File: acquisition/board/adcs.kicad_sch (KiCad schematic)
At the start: 108 parts, among them U1 AD9251, U13 ICE40UP5K_QFN48, U2 XC7A50T-1FTG256C, U3 AD9251, U4 AD9251, U5 AD9251, U6 ICE40UP5K_QFN48

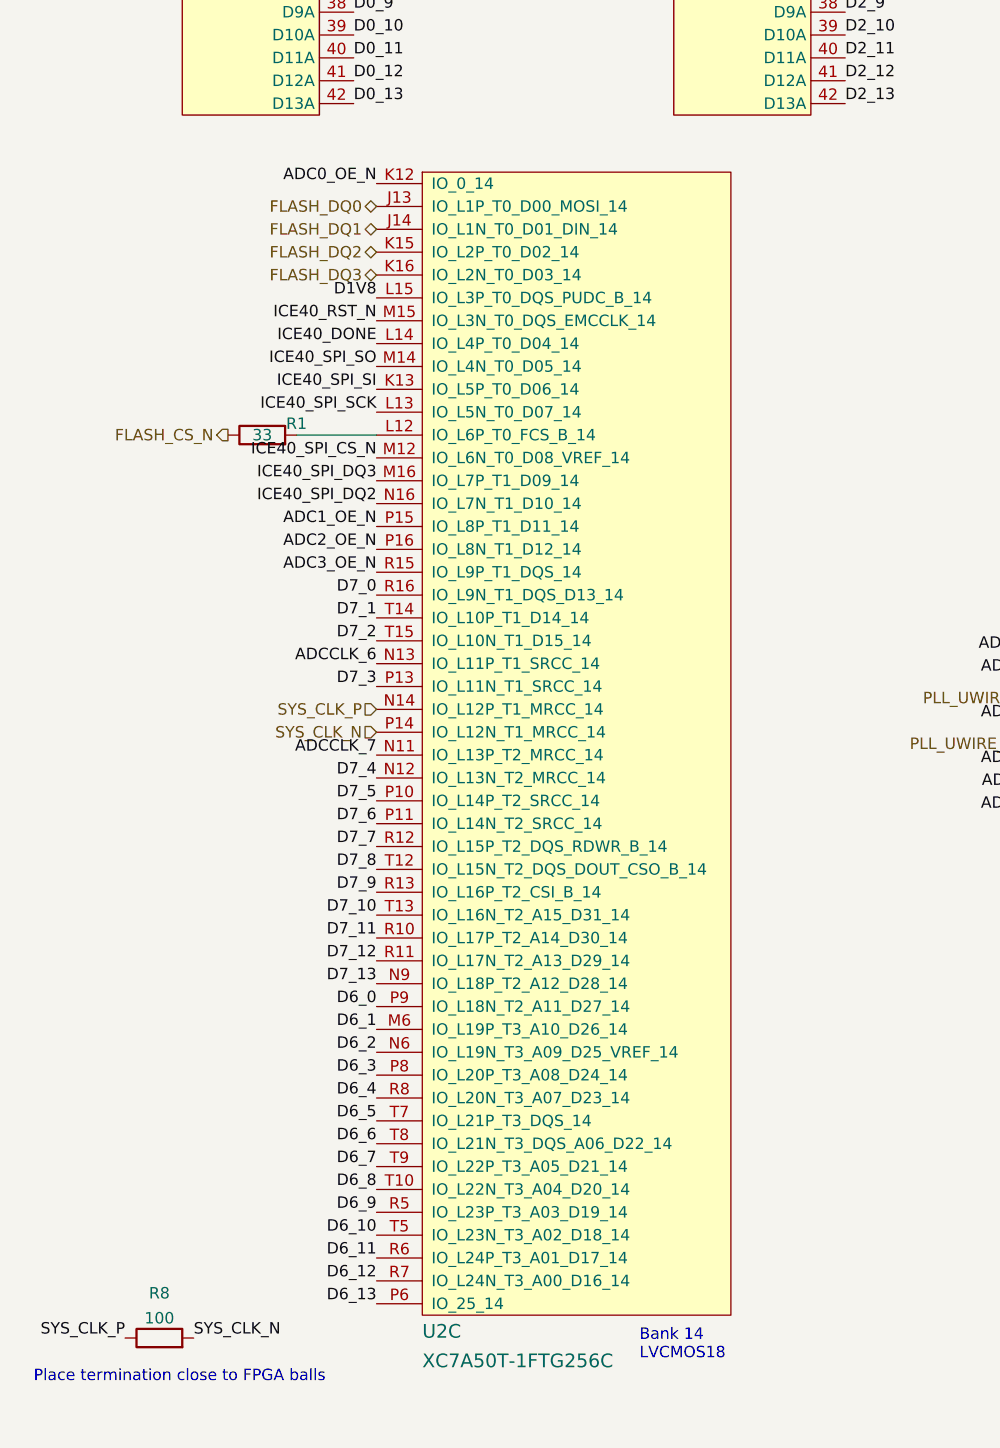
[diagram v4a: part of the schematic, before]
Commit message: Completed schematic after design review, ready for layout
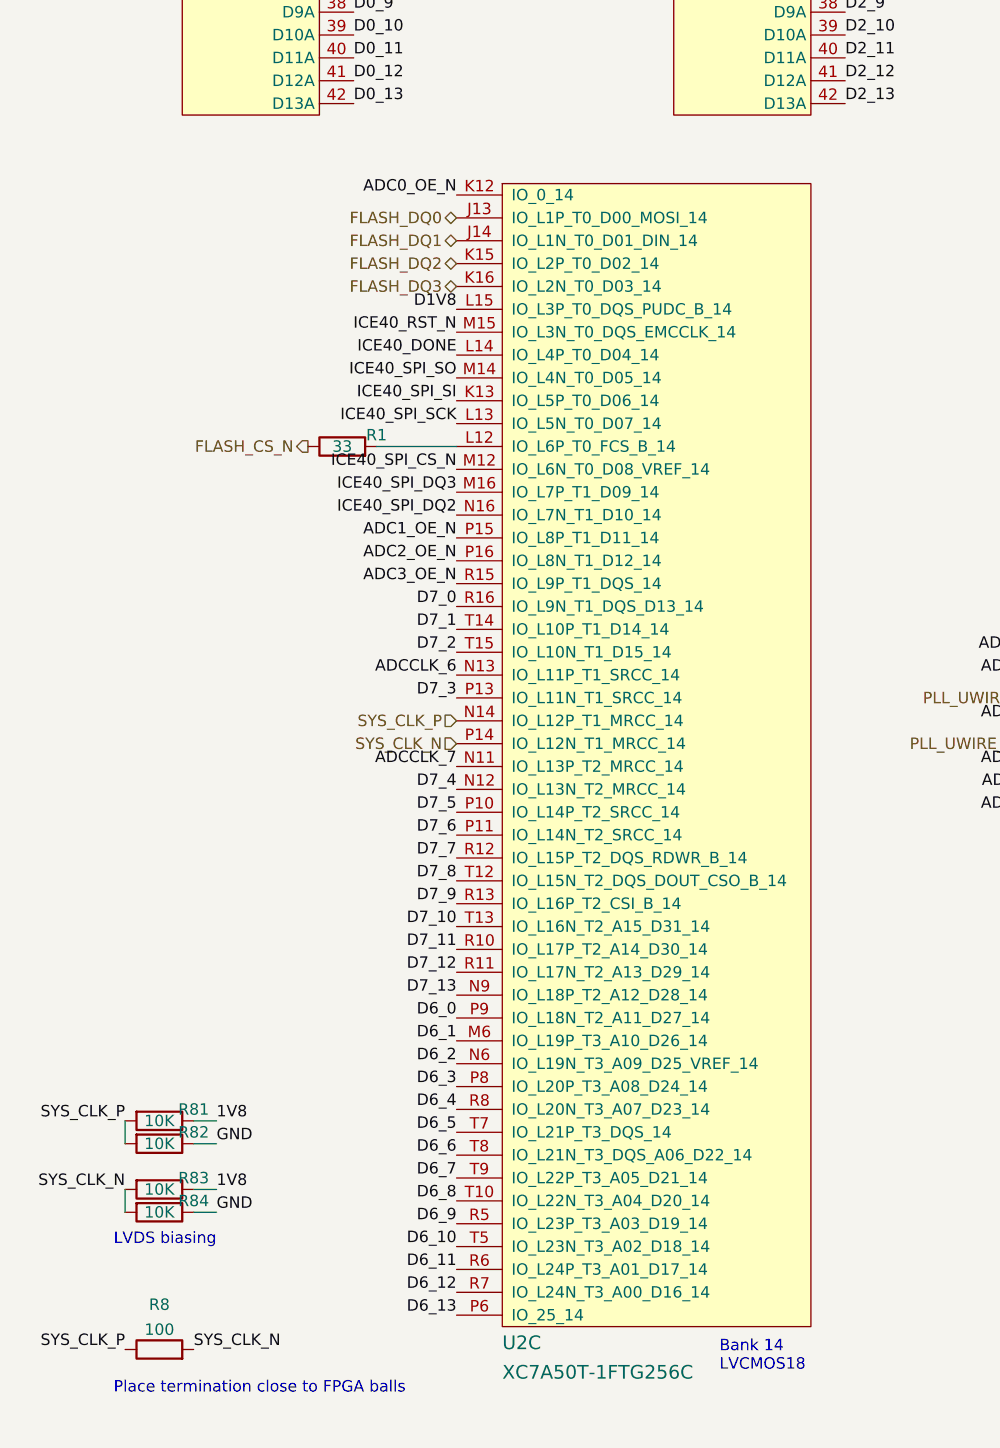
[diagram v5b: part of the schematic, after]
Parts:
- added R81, R82, R83, R84: 10K, azonenberg_pcb:EIA_0402_RES_NOSILK, symbol device:R
- C202, C203, C204, C205: footprint (none) -> azonenberg_pcb:EIA_0603_CAP_NOSILK
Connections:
- net 1V8: now also R81.1, R83.1
- net GND: now also R82.1, R84.1
- net SYS_CLK_N: now also R83.2, R84.2
- net SYS_CLK_P: now also R81.2, R82.2
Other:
- note added: "LVDS biasing"
- moved on the sheet: R1, R8, U2C

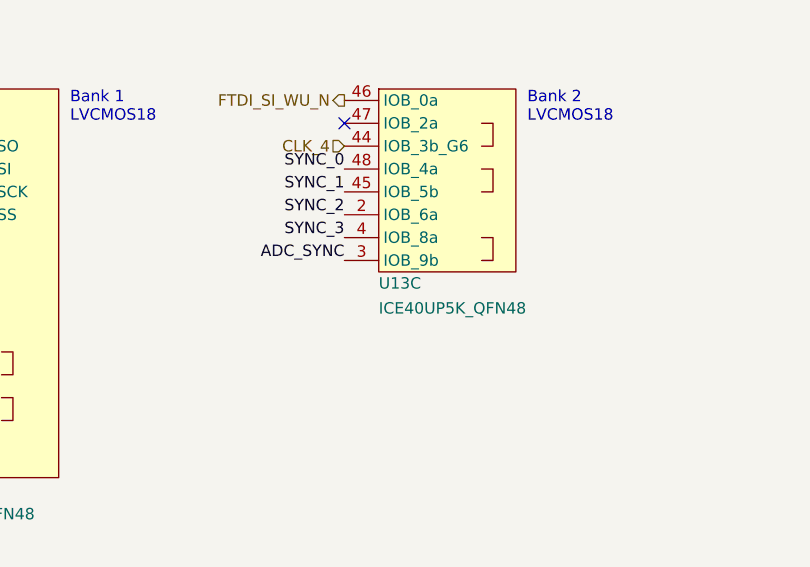
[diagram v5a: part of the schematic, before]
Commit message: Finished footprint assignment
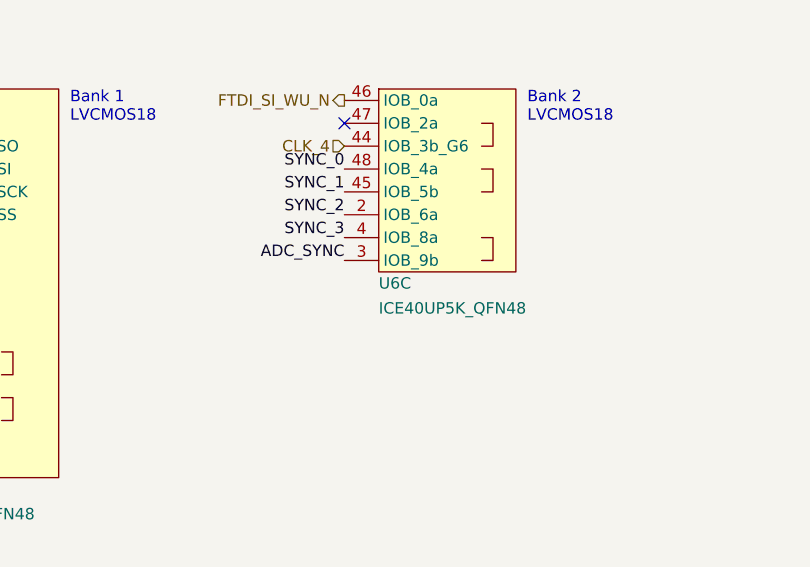
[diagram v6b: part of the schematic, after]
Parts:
- U1, U3, U4, U5: footprint (none) -> azonenberg_pcb:QFN_64_0.5MM_9x9MM
- U6: renamed from U13; footprint (none) -> azonenberg_pcb:QFN_48_0.5MM_7x7MM
- U6: footprint (none) -> azonenberg_pcb:QFN_48_0.5MM_7x7MM
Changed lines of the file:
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@@
   (title_block
     (title "Digitizer board")
-    (date "2022-07-17")
+    (date "2023-01-29")
     (rev "0.1")
     (company "A. Zonenberg")
@@
   (symbol (lib_id "lattice-azonenberg:ICE40UP5K_QFN48") (at 316.23 245.11 0) (unit 3)
     (in_bom yes) (on_board yes)
-    (property "Reference" "U13" (id 0) (at 316.23 246.38 0)
+    (property "Reference" "U6" (id 0) (at 316.23 246.38 0)
       (effects (font (size 1.27 1.27)) (justify left))
     )
@@
       (effects (font (size 1.27 1.27)) (justify left))
     )
-    (property "Footprint" "" (id 2) (at 316.23 245.11 0)
+    (property "Footprint" "azonenberg_pcb:QFN_48_0.5MM_7x7MM" (id 2) (at 316.23 245.11 0)
       (effects (font (size 1.27 1.27)) hide)
     )
@@
     (property "Reference" "U3" (id 0) (at 97.79 17.6743 0))
     (property "Value" "AD9251" (id 1) (at 97.79 20.4494 0))
-    (property "Footprint" "" (id 2) (at 87.63 86.36 0)
+    (property "Footprint" "azonenberg_pcb:QFN_64_0.5MM_9x9MM" (id 2) (at 87.63 86.36 0)
       (effects (font (size 1.27 1.27)) hide)
     )
@@
     (property "Reference" "U3" (id 0) (at 316.23 72.2843 0))
     (property "Value" "AD9251" (id 1) (at 316.23 75.0594 0))
-    (property "Footprint" "" (id 2) (at 308.61 121.92 0)
+    (property "Footprint" "azonenberg_pcb:QFN_64_0.5MM_9x9MM" (id 2) (at 308.61 121.92 0)
       (effects (font (size 1.27 1.27)) hide)
     )
@@
     (property "Reference" "U4" (id 0) (at 152.4 17.6743 0))
     (property "Value" "AD9251" (id 1) (at 152.4 20.4494 0))
-    (property "Footprint" "" (id 2) (at 142.24 86.36 0)
+    (property "Footprint" "azonenberg_pcb:QFN_64_0.5MM_9x9MM" (id 2) (at 142.24 86.36 0)
       (effects (font (size 1.27 1.27)) hide)
     )
@@
     (property "Reference" "U1" (id 0) (at 43.18 17.6743 0))
     (property "Value" "AD9251" (id 1) (at 43.18 20.4494 0))
-    (property "Footprint" "" (id 2) (at 33.02 86.36 0)
+    (property "Footprint" "azonenberg_pcb:QFN_64_0.5MM_9x9MM" (id 2) (at 33.02 86.36 0)
       (effects (font (size 1.27 1.27)) hide)
     )
@@
     (property "Reference" "U1" (id 0) (at 316.23 18.9443 0))
     (property "Value" "AD9251" (id 1) (at 316.23 21.7194 0))
-    (property "Footprint" "" (id 2) (at 308.61 68.58 0)
+    (property "Footprint" "azonenberg_pcb:QFN_64_0.5MM_9x9MM" (id 2) (at 308.61 68.58 0)
       (effects (font (size 1.27 1.27)) hide)
     )
@@
     (property "Reference" "U3" (id 0) (at 95.25 88.7943 0))
     (property "Value" "AD9251" (id 1) (at 95.25 91.5694 0))
-    (property "Footprint" "" (id 2) (at 87.63 138.43 0)
+    (property "Footprint" "azonenberg_pcb:QFN_64_0.5MM_9x9MM" (id 2) (at 87.63 138.43 0)
       (effects (font (size 1.27 1.27)) hide)
     )
@@
     (property "Reference" "U4" (id 0) (at 370.84 18.9443 0))
     (property "Value" "AD9251" (id 1) (at 370.84 21.7194 0))
-    (property "Footprint" "" (id 2) (at 363.22 68.58 0)
+    (property "Footprint" "azonenberg_pcb:QFN_64_0.5MM_9x9MM" (id 2) (at 363.22 68.58 0)
       (effects (font (size 1.27 1.27)) hide)
     )
@@
     (property "Reference" "U5" (id 0) (at 370.84 72.2843 0))
     (property "Value" "AD9251" (id 1) (at 370.84 75.0594 0))
-    (property "Footprint" "" (id 2) (at 363.22 121.92 0)
+    (property "Footprint" "azonenberg_pcb:QFN_64_0.5MM_9x9MM" (id 2) (at 363.22 121.92 0)
       (effects (font (size 1.27 1.27)) hide)
     )
@@
     (property "Reference" "U5" (id 0) (at 204.47 88.7943 0))
     (property "Value" "AD9251" (id 1) (at 204.47 91.5694 0))
-    (property "Footprint" "" (id 2) (at 196.85 138.43 0)
+    (property "Footprint" "azonenberg_pcb:QFN_64_0.5MM_9x9MM" (id 2) (at 196.85 138.43 0)
       (effects (font (size 1.27 1.27)) hide)
     )
@@
     (property "Reference" "U4" (id 0) (at 149.86 88.7943 0))
     (property "Value" "AD9251" (id 1) (at 149.86 91.5694 0))
-    (property "Footprint" "" (id 2) (at 142.24 138.43 0)
+    (property "Footprint" "azonenberg_pcb:QFN_64_0.5MM_9x9MM" (id 2) (at 142.24 138.43 0)
       (effects (font (size 1.27 1.27)) hide)
     )
@@
     (property "Reference" "U1" (id 0) (at 40.64 88.7943 0))
     (property "Value" "AD9251" (id 1) (at 40.64 91.5694 0))
-    (property "Footprint" "" (id 2) (at 33.02 138.43 0)
+    (property "Footprint" "azonenberg_pcb:QFN_64_0.5MM_9x9MM" (id 2) (at 33.02 138.43 0)
       (effects (font (size 1.27 1.27)) hide)
     )
@@
       (effects (font (size 1.27 1.27)) (justify left))
     )
-    (property "Footprint" "" (id 2) (at 261.62 267.97 0)
+    (property "Footprint" "azonenberg_pcb:QFN_48_0.5MM_7x7MM" (id 2) (at 261.62 267.97 0)
       (effects (font (size 1.27 1.27)) hide)
     )
@@
     (property "Reference" "U5" (id 0) (at 207.01 17.6743 0))
     (property "Value" "AD9251" (id 1) (at 207.01 20.4494 0))
-    (property "Footprint" "" (id 2) (at 196.85 86.36 0)
+    (property "Footprint" "azonenberg_pcb:QFN_64_0.5MM_9x9MM" (id 2) (at 196.85 86.36 0)
       (effects (font (size 1.27 1.27)) hide)
     )
